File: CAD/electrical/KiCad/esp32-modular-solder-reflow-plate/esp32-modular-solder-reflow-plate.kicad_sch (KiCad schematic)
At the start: 58 parts, among them J4 TB003-500-P02BE, J5 I2C, J6 Micro_SD, J7 USB-C, SW1 µC_BTN01, SW2 µC_BTN02, SW3 µC_BTN03, SW4 µC_BTN04, SW5 µC_EN, SW6 µC_IO0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

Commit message: - CAD: schematic improvements
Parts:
- removed C10, C11, C13, C14, C15, C16: 1µ, Capacitor_SMD:C_0603_1608Metric_Pad1.08x0.95mm_HandSolder, symbol Device:C_Small
- removed C12, C17: 100n, Capacitor_SMD:C_0603_1608Metric_Pad1.08x0.95mm_HandSolder, symbol Device:C_Small
- removed C24: 10nF, Capacitor_SMD:C_0603_1608Metric, symbol Device:C
- removed C8: 100nF, Capacitor_SMD:C_0603_1608Metric, symbol Device:C
- removed C9: 4µ7, Capacitor_SMD:C_0603_1608Metric_Pad1.08x0.95mm_HandSolder, symbol Device:C_Small
- removed D11: SK6805, LED_SMD:LED_RGB_5050-6, symbol LED:SK6805
- removed D12: LED_B, LED_SMD:LED_0603_1608Metric_Pad1.05x0.95mm_HandSolder, symbol Device:LED
- removed D13: LED_GR, LED_SMD:LED_0603_1608Metric_Pad1.05x0.95mm_HandSolder, symbol Device:LED
- removed D14, D15, D16: LED_R, LED_SMD:LED_0603_1608Metric_Pad1.05x0.95mm_HandSolder, symbol Device:LED
- removed D3: REV_CUR_PROT, symbol Device:D_Schottky
- removed J4: TB003-500-P02BE, library_manager:SHDR2W100P0X500_1X2_1000X780X1030P, symbol library_loader:TB003-500-P02BE
- removed J5: I2C, Connector_PinSocket_2.54mm:PinSocket_1x05_P2.54mm_Vertical, symbol Connector_Generic:Conn_01x05
- removed J6: Micro_SD, Connector_Card:microSD_HC_Hirose_DM3D-SF, symbol Connector:Micro_SD_Card_Det
- removed J7: USB-C, Connector_USB:USB_C_Receptacle_GCT_USB4085, symbol Connector:USB_C_Receptacle_USB2.0
- removed L1: Ferrite bead, Inductor_SMD:L_0603_1608Metric_Pad1.05x0.95mm_HandSolder, symbol Device:L_Ferrite_Small
- removed R10, R17, R25: 10k, Resistor_SMD:R_0603_1608Metric_Pad0.98x0.95mm_HandSolder, symbol Device:R_Small
- removed R11, R12: 5k1, symbol Device:R_Small
- removed R13, R14, R15, R16, R27, R28, R29, R3, R5, R8, R9: 330, Resistor_SMD:R_0603_1608Metric_Pad0.98x0.95mm_HandSolder, symbol Device:R_Small
- removed R21, R22, R23, R24, R26: 0, Resistor_SMD:R_0603_1608Metric_Pad0.98x0.95mm_HandSolder, symbol Device:R_Small
- removed SW1: µC_BTN01, Button_Switch_THT:SW_PUSH_6mm, symbol Switch:SW_Push
- removed SW2: µC_BTN02, Button_Switch_THT:SW_PUSH_6mm, symbol Switch:SW_Push
- removed SW3: µC_BTN03, Button_Switch_THT:SW_PUSH_6mm, symbol Switch:SW_Push
- removed SW4: µC_BTN04, Button_Switch_THT:SW_PUSH_6mm, symbol Switch:SW_Push
- removed SW5: µC_EN, Button_Switch_THT:SW_PUSH_6mm, symbol Switch:SW_Push
- removed SW6: µC_IO0, Button_Switch_THT:SW_PUSH_6mm, symbol Switch:SW_Push
- added C2: 10n, symbol Device:C_Small
- added C6: 100n, symbol Device:C_Small
- added U1: ESP32-S3-WROOM-1, Espressif:ESP32-S3-WROOM-1, symbol espressif-kicad-lib:ESP32-S3-WROOM-1
- renumbered C26 to C1, C27 to C3, C28 to C4, C6 to C5, U4 to U3, Y2 to Y1
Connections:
- net FLASH is gone; now on net IO0: U3.27 (GPIO0/BOOT)
- net tempCS is gone; now on net ADC_TEMP_CS: U2.6 (~{CS})
- net tempSCK is gone; now on net ADC_TEMP_SCK: U2.5 (SCK)
- net tempSO is gone; now on net ADC_TEMP_SO: U2.7 (SO)
- net +3V3: now also C6.1; no longer U3.3 (EN)
- net ADC_TEMP_CS: now also U3.16 (GPIO46); no longer U3.31 (GPIO38/FSPIWP/SUBSPIWP)
- net ADC_TEMP_SCK: now also U3.25 (GPIO48/SPICLK_N/SUBSPICLK_N_DIFF)
- net ADC_TEMP_SO: now also U3.24 (GPIO47/SPICLK_P/SUBSPICLK_P_DIFF)
- net BTN01: now also U3.32 (MTCK/GPIO39/CLK_OUT3/SUBSPICS1)
- net BTN02: now also U3.33 (MTDO/GPIO40/CLK_OUT2)
- net BTN03: now also U3.34 (MTDI/GPIO41/CLK_OUT1)
- net BTN04: now also U3.35 (MTMS/GPIO42)
- net EN: now also U3.3 (EN)
- net GND: now also U3.1 (GND), U3.40 (GND), U3.41 (GND), C6.2
- net HEATER_CTRL: now also U3.12 (GPIO8/TOUCH8/ADC1_CH7/SUBSPICS1); no longer U3.18 (GPIO10/TOUCH10/ADC1_CH9/FSPICS0/FSPIIO4/SUBSPICS0)
- net I2C_SCL: now also U3.38 (GPIO2/TOUCH2/ADC1_CH1); no longer U3.15 (GPIO3/TOUCH3/ADC1_CH2)
- net I2C_SDA: now also U3.15 (GPIO3/TOUCH3/ADC1_CH2); no longer U3.4 (GPIO4/TOUCH4/ADC1_CH3)
- net LED_1: now also U3.6 (GPIO6/TOUCH6/ADC1_CH5); no longer U3.12 (GPIO8/TOUCH8/ADC1_CH7/SUBSPICS1)
- net LED_2: now also U3.7 (GPIO7/TOUCH7/ADC1_CH6); no longer U3.17 (GPIO9/TOUCH9/ADC1_CH8/FSPIHD/SUBSPIHD)
- net NEOPIXEL_DIN: now also U3.5 (GPIO5/TOUCH5/ADC1_CH4); no longer U3.7 (GPIO7/TOUCH7/ADC1_CH6)
- net SD_CD: now also U3.19 (GPIO11/TOUCH11/ADC2_CH0/FSPID/FSPIIO5/SUBSPID); no longer U3.21 (GPIO13/TOUCH13/ADC2_CH2/FSPIQ/FSPIIO7/SUBSPIQ)
- net SD_CLK: now also U3.20 (GPIO12/TOUCH12/ADC2_CH1/FSPICLK/FSPIIO6/SUBSPICLK); no longer U3.22 (GPIO14/TOUCH14/ADC2_CH3/FSPIWP/FSPIDQS/SUBSPIWP)
- net SD_CMD: now also U3.21 (GPIO13/TOUCH13/ADC2_CH2/FSPIQ/FSPIIO7/SUBSPIQ); no longer U3.10 (GPIO17/U1TXD/ADC2_CH6)
- net SD_DAT0: now also U3.22 (GPIO14/TOUCH14/ADC2_CH3/FSPIWP/FSPIDQS/SUBSPIWP); no longer U3.11 (GPIO18/U1RXD/ADC2_CH7/CLK_OUT3)
- net SD_DET: now also U3.18 (GPIO10/TOUCH10/ADC1_CH9/FSPICS0/FSPIIO4/SUBSPICS0); no longer U3.20 (GPIO12/TOUCH12/ADC2_CH1/FSPICLK/FSPIIO6/SUBSPICLK)
- net RX0: now reaches U3.36 (U0RXD/GPIO44/CLK_OUT2)
- net TX0: now reaches U3.37 (U0TXD/GPIO43/CLK_OUT1)
- net THCPL_p: now reaches U2.3 (T+)
- net THCPL_p: now also C2.2
- net THCPL_n: now reaches U2.2 (T-)
- net THCPL_n: now also C2.1
- net VccDiv: no longer names the net of U3.39 (GPIO1/TOUCH1/ADC1_CH0)
- new net: U1.1 (GND), U1.40 (GND), U1.41 (GND)
- no-connect marks 17 -> 8
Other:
- added sheet Input Output (input_output.kicad_sch)
- note removed: "BUTTONS"
- note removed: "CONNECTORS"
- note removed: "LEDS"
- note removed: "SD-CARD"
- title: (none) -> Modular Solder Reflow PCB

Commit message: - CAD: initial routed pcb
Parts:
- removed C3: 1µ, symbol Device:C_Small
- removed U1: ESP32-S3-WROOM-1, Espressif:ESP32-S3-WROOM-1, symbol espressif-kicad-lib:ESP32-S3-WROOM-1
- C1, C2: footprint (none) -> Capacitor_SMD:C_0603_1608Metric_Pad1.08x0.95mm_HandSolder
- C3: renamed from C4; footprint (none) -> Capacitor_SMD:C_0603_1608Metric_Pad1.08x0.95mm_HandSolder
- C4: renamed from C5; footprint (none) -> Capacitor_SMD:C_0603_1608Metric_Pad1.08x0.95mm_HandSolder
- C5: renamed from C6; footprint (none) -> Capacitor_SMD:C_0603_1608Metric_Pad1.08x0.95mm_HandSolder
- C6: renamed from C7; footprint (none) -> Capacitor_SMD:C_0603_1608Metric_Pad1.08x0.95mm_HandSolder
- Y1: footprint (none) -> Crystal:Crystal_SMD_3225-4Pin_3.2x2.5mm_HandSoldering
- renumbered U2 to U1, U3 to U2
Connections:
- net LED_1 is gone; now on net NEOPIXEL_DIN: U2.6 (GPIO6/TOUCH6/ADC1_CH5)
- net LED_2 is gone; now on net ADC_TEMP_SCK: U2.7 (GPIO7/TOUCH7/ADC1_CH6)
- net ADC_TEMP_CS: now also U2.10 (GPIO17/U1TXD/ADC2_CH6); no longer U2.16 (GPIO46)
- net ADC_TEMP_SCK: no longer U2.25 (GPIO48/SPICLK_N/SUBSPICLK_N_DIFF)
- net ADC_TEMP_SO: now also U2.11 (GPIO18/U1RXD/ADC2_CH7/CLK_OUT3); no longer U2.24 (GPIO47/SPICLK_P/SUBSPICLK_P_DIFF)
- net I2C_SCL: now also U2.5 (GPIO5/TOUCH5/ADC1_CH4); no longer U2.38 (GPIO2/TOUCH2/ADC1_CH1)
- net I2C_SDA: now also U2.4 (GPIO4/TOUCH4/ADC1_CH3); no longer U2.15 (GPIO3/TOUCH3/ADC1_CH2)
- net NEOPIXEL_DIN: no longer U2.5 (GPIO5/TOUCH5/ADC1_CH4)
- net RX0: now also U2.26 (GPIO45); no longer U2.36 (U0RXD/GPIO44/CLK_OUT2)
- net SD_CD: now also U2.18 (GPIO10/TOUCH10/ADC1_CH9/FSPICS0/FSPIIO4/SUBSPICS0); no longer U2.19 (GPIO11/TOUCH11/ADC2_CH0/FSPID/FSPIIO5/SUBSPID)
- net SD_CLK: now also U2.21 (GPIO13/TOUCH13/ADC2_CH2/FSPIQ/FSPIIO7/SUBSPIQ); no longer U2.20 (GPIO12/TOUCH12/ADC2_CH1/FSPICLK/FSPIIO6/SUBSPICLK)
- net SD_CMD: now also U2.20 (GPIO12/TOUCH12/ADC2_CH1/FSPICLK/FSPIIO6/SUBSPICLK); no longer U2.21 (GPIO13/TOUCH13/ADC2_CH2/FSPIQ/FSPIIO7/SUBSPIQ)
- net SD_DET: now also U2.19 (GPIO11/TOUCH11/ADC2_CH0/FSPID/FSPIIO5/SUBSPID); no longer U2.18 (GPIO10/TOUCH10/ADC1_CH9/FSPICS0/FSPIIO4/SUBSPICS0)
- net TX0: now also U2.25 (GPIO48/SPICLK_N/SUBSPICLK_N_DIFF); no longer U2.37 (U0TXD/GPIO43/CLK_OUT1)
- no-connect marks 8 -> 10
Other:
- moved on the sheet: C3, C4, C6, Y1

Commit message: - cad: improved routing; added VIN voltage monitoring capability
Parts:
- added R1: 100M, Resistor_SMD:R_0603_1608Metric_Pad0.98x0.95mm_HandSolder, symbol Device:R_Small
- added R2: 15M, Resistor_SMD:R_0603_1608Metric_Pad0.98x0.95mm_HandSolder, symbol Device:R_Small
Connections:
- net GND: now also R2.2
- net VIN_ADC: now reaches U2.15 (GPIO3/TOUCH3/ADC1_CH2)
- net VIN_ADC: now also R1.2, R2.1
- new net VCC_PWR: R1.1
- no-connect marks 10 -> 9
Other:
- note added: "Ensure to use appropriate voltage devider values!"
- note added: "VIN-Monitoring"
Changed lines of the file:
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@@
   (junction (at 67.31 143.51) (diameter 0) (color 0 0 0 0)
   )
+  (junction (at 109.22 165.1) (diameter 0) (color 0 0 0 0)
+  )
   (no_connect (at 127 52.07))
-  (no_connect (at 127 54.61))
   (no_connect (at 127 92.71))
   (no_connect (at 127 69.85))
@@
     (stroke (width 0) (type default))
   )
+  (wire (pts (xy 106.68 165.1) (xy 109.22 165.1))
+    (stroke (width 0) (type default))
+  )
+  (wire (pts (xy 109.22 167.64) (xy 109.22 165.1))
+    (stroke (width 0) (type default))
+  )
   (polyline (pts (xy 149.86 15.24) (xy 149.86 119.38))
     (stroke (width 0) (type default))
@@
     (stroke (width 0) (type default))
   )
+  (polyline (pts (xy 123.19 156.21) (xy 123.19 176.53))
+    (stroke (width 0) (type default))
+  )
   (wire (pts (xy 30.48 177.8) (xy 30.48 180.34))
     (stroke (width 0) (type default))
@@
     (stroke (width 0) (type default))
   )
+  (wire (pts (xy 99.06 165.1) (xy 101.6 165.1))
+    (stroke (width 0) (type default))
+  )
   (wire (pts (xy 62.23 128.27) (xy 67.31 128.27))
     (stroke (width 0) (type default))
@@
     (stroke (width 0) (type default))
   )
+  (polyline (pts (xy 123.19 176.53) (xy 85.09 176.53))
+    (stroke (width 0) (type default))
+  )
   (polyline (pts (xy 82.55 156.21) (xy 15.24 156.21))
     (stroke (width 0) (type default))
@@
     (stroke (width 0) (type default))
   )
+  (wire (pts (xy 127 54.61) (xy 129.54 54.61))
+    (stroke (width 0) (type default))
+  )
   (wire (pts (xy 33.02 41.91) (xy 35.56 41.91))
     (stroke (width 0) (type default))
@@
     (stroke (width 0) (type default))
   )
+  (wire (pts (xy 109.22 165.1) (xy 111.76 165.1))
+    (stroke (width 0) (type default))
+  )
   (polyline (pts (xy 15.24 153.67) (xy 15.24 121.92))
     (stroke (width 0) (type default))
@@
     (stroke (width 0) (type default))
   )
+  (wire (pts (xy 116.84 165.1) (xy 119.38 165.1))
+    (stroke (width 0) (type default))
+  )
   (wire (pts (xy 41.91 162.56) (xy 41.91 163.83))
     (stroke (width 0) (type default))
@@
     (stroke (width 0) (type default))
   )
+  (polyline (pts (xy 85.09 156.21) (xy 123.19 156.21))
+    (stroke (width 0) (type default))
+  )
   (wire (pts (xy 127 74.93) (xy 129.54 74.93))
     (stroke (width 0) (type default))
@@
     (stroke (width 0) (type default))
   )
+  (wire (pts (xy 119.38 165.1) (xy 119.38 167.64))
+    (stroke (width 0) (type default))
+  )
   (polyline (pts (xy 15.24 15.24) (xy 15.24 119.38))
     (stroke (width 0) (type default))
@@
     (stroke (width 0) (type default))
   )
+  (wire (pts (xy 99.06 167.64) (xy 109.22 167.64))
+    (stroke (width 0) (type default))
+  )
   (wire (pts (xy 33.02 24.13) (xy 81.28 24.13))
+    (stroke (width 0) (type default))
+  )
+  (polyline (pts (xy 85.09 156.21) (xy 85.09 176.53))
     (stroke (width 0) (type default))
   )
@@
     (effects (font (size 1.27 1.27)) (justify left bottom))
   )
+  (text "Ensure to use appropriate \nvoltage devider values!" (exclude_from_sim no)
+    (at 88.9 173.99 0)
+    (effects (font (size 1.27 1.27) (thickness 0.254) bold (color 255 0 13 1)) (justify left bottom))
+  )
   (text "µC-PASSIVES\n" (exclude_from_sim no)
  (at 17.78 125.73 0)
     (effects (font (size 1.27 1.27) (thickness 0.254) bold) (justify left bottom))
   )
+  (text "VIN-Monitoring\n" (exclude_from_sim no)
+ (at 87.63 160.02 0)
+    (effects (font (size 1.27 1.27) (thickness 0.254) bold) (justify left bottom))
+  )
   (text "µC\n" (exclude_from_sim no)
  (at 17.78 19.05 0)
@@
     )
   )
+  (global_label "VIN_ADC" (shape output) (at 99.06 167.64 180) (fields_autoplaced)
+    (effects (font (size 1.27 1.27)) (justify right))
+    (property "Intersheetrefs" "${INTERSHEET_REFS}" (at 88.5341 167.64 0)
+      (effects (font (size 1.27 1.27)) (justify right) hide)
+    )
+  )
   (global_label "BTN03" (shape input) (at 33.02 52.07 180) (fields_autoplaced)
     (effects (font (size 1.27 1.27)) (justify right))
@@
     )
   )
+  (global_label "VCC_PWR" (shape input) (at 99.06 165.1 180) (fields_autoplaced)
+    (effects (font (size 1.27 1.27)) (justify right))
+    (property "Intersheetrefs" "${INTERSHEET_REFS}" (at 87.5666 165.1 0)
+      (effects (font (size 1.27 1.27)) (justify right) hide)
+    )
+  )
   (global_label "XTAL_P" (shape bidirectional) (at 57.15 134.62 180) (fields_autoplaced)
     (effects (font (size 1.27 1.27)) (justify right))
@@
     (effects (font (size 1.27 1.27)) (justify left))
     (property "Intersheetrefs" "${INTERSHEET_REFS}" (at 140.4286 82.55 0)
+      (effects (font (size 1.27 1.27)) (justify left) hide)
+    )
+  )
+  (global_label "VIN_ADC" (shape input) (at 129.54 54.61 0) (fields_autoplaced)
+    (effects (font (size 1.27 1.27)) (justify left))
+    (property "Intersheetrefs" "${INTERSHEET_REFS}" (at 140.0659 54.61 0)
       (effects (font (size 1.27 1.27)) (justify left) hide)
     )
@@
     )
   )
+  (symbol (lib_id "Device:R_Small") (at 104.14 165.1 90) (unit 1)
+    (in_bom yes) (on_board yes) (dnp no)
+    (property "Reference" "R1" (at 101.6 162.56 90)
+      (effects (font (size 1.27 1.27)))
+    )
+    (property "Value" "100M" (at 106.68 162.56 90)
+      (effects (font (size 1.27 1.27)))
+    )
+    (property "Footprint" "Resistor_SMD:R_0603_1608Metric_Pad0.98x0.95mm_HandSolder" (at 104.14 165.1 0)
+      (effects (font (size 1.27 1.27)) hide)
+    )
+    (property "Datasheet" "~" (at 104.14 165.1 0)
+      (effects (font (size 1.27 1.27)) hide)
+    )
+    (pin "1")
+    (pin "2")
+    (instances
+      (project "esp32-modular-solder-reflow-plate"
+        (path "/33f3a99a-8df0-41a5-be2d-1e3400ca68bb"
+          (reference "R1") (unit 1)
+        )
+        (path "/33f3a99a-8df0-41a5-be2d-1e3400ca68bb/9103847b-7285-41f5-846d-96de7eb793c2"
+          (reference "R?") (unit 1)
+        )
+      )
+      (project "dspctl_esp32_r0"
+        (path "/8b3186b5-4efc-4a83-b981-ca6a69ceeadc"
+          (reference "R?") (unit 1)
+        )
+        (path "/8b3186b5-4efc-4a83-b981-ca6a69ceeadc/5662498d-5991-4f3b-8484-1c94b706ac61"
+          (reference "R?") (unit 1)
+        )
+      )
+    )
+  )
+  (symbol (lib_id "Device:R_Small") (at 114.3 165.1 90) (unit 1)
+    (in_bom yes) (on_board yes) (dnp no)
+    (property "Reference" "R2" (at 113.03 162.56 90)
+      (effects (font (size 1.27 1.27)))
+    )
+    (property "Value" "15M" (at 118.11 162.56 90)
+      (effects (font (size 1.27 1.27)))
+    )
+    (property "Footprint" "Resistor_SMD:R_0603_1608Metric_Pad0.98x0.95mm_HandSolder" (at 114.3 165.1 0)
+      (effects (font (size 1.27 1.27)) hide)
+    )
+    (property "Datasheet" "~" (at 114.3 165.1 0)
+      (effects (font (size 1.27 1.27)) hide)
+    )
+    (pin "1")
+    (pin "2")
+    (instances
+      (project "esp32-modular-solder-reflow-plate"
+        (path "/33f3a99a-8df0-41a5-be2d-1e3400ca68bb"
+          (reference "R2") (unit 1)
+        )
+        (path "/33f3a99a-8df0-41a5-be2d-1e3400ca68bb/9103847b-7285-41f5-846d-96de7eb793c2"
+          (reference "R?") (unit 1)
+        )
+      )
+      (project "dspctl_esp32_r0"
+        (path "/8b3186b5-4efc-4a83-b981-ca6a69ceeadc"
+          (reference "R?") (unit 1)
+        )
+        (path "/8b3186b5-4efc-4a83-b981-ca6a69ceeadc/5662498d-5991-4f3b-8484-1c94b706ac61"
+          (reference "R?") (unit 1)
+        )
+      )
+    )
+  )
   (symbol (lib_id "power:GND") (at 62.23 129.54 0) (unit 1)
     (in_bom yes) (on_board yes) (dnp no)
@@
         )
       )
+    )
+  )
+  (symbol (lib_id "power:GND") (at 119.38 167.64 0) (unit 1)
+    (in_bom yes) (on_board yes) (dnp no)
+    (property "Reference" "#PWR09" (at 119.38 173.99 0)
+      (effects (font (size 1.27 1.27)) hide)
+    )
+    (property "Value" "GND" (at 119.38 171.45 0)
+      (effects (font (size 1.27 1.27)))
+    )
+    (property "Footprint" "" (at 119.38 167.64 0)
+      (effects (font (size 1.27 1.27)) hide)
+    )
+    (property "Datasheet" "" (at 119.38 167.64 0)
+      (effects (font (size 1.27 1.27)) hide)
+    )
+    (pin "1")
+    (instances
+      (project "esp32-modular-solder-reflow-plate"
+        (path "/33f3a99a-8df0-41a5-be2d-1e3400ca68bb"
+          (reference "#PWR09") (unit 1)
+        )
+        (path "/33f3a99a-8df0-41a5-be2d-1e3400ca68bb/9103847b-7285-41f5-846d-96de7eb793c2"
+          (reference "#PWR?") (unit 1)
+        )
+      )

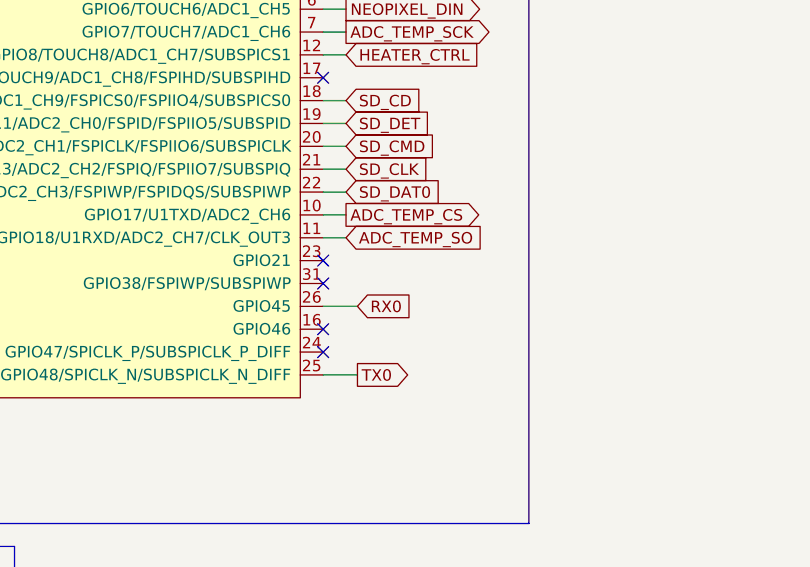
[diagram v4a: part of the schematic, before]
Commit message: - cad: added a buzzer control output
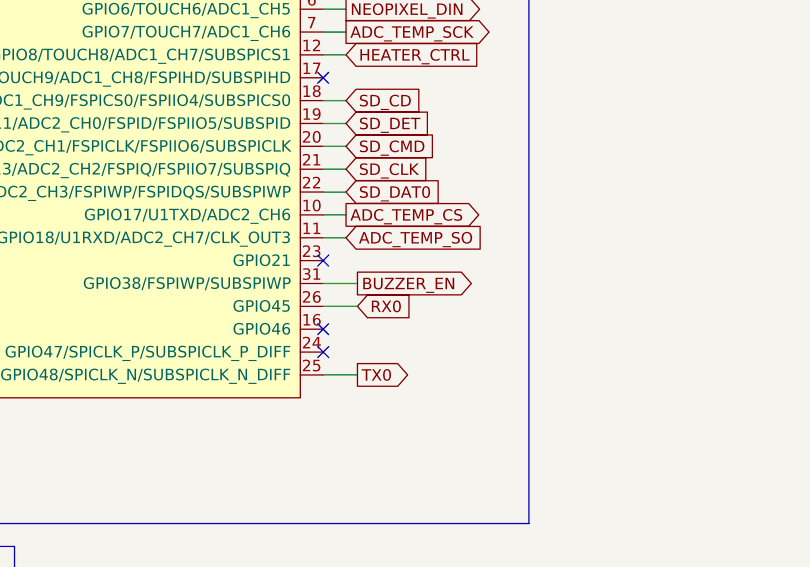
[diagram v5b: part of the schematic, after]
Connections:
- net BUZZER_EN: now reaches U2.31 (GPIO38/FSPIWP/SUBSPIWP)
- no-connect marks 9 -> 8
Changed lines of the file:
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@@
   )
   (no_connect (at 127 52.07))
-  (no_connect (at 127 92.71))
   (no_connect (at 127 69.85))
   (no_connect (at 127 34.29))
@@
     (stroke (width 0) (type default))
   )
+  (wire (pts (xy 127 92.71) (xy 130.81 92.71))
+    (stroke (width 0) (type default))
+  )
   (wire (pts (xy 77.47 143.51) (xy 77.47 142.24))
     (stroke (width 0) (type default))
@@
       (effects (font (size 1.27 1.27)) (justify left) hide)
     )
+  )
+  (global_label "BUZZER_EN" (shape output) (at 130.81 92.71 0) (fields_autoplaced)
+    (effects (font (size 1.27 1.27)) (justify left))
+    (property "Intersheetrefs" "${INTERSHEET_REFS}" (at 144.6014 92.71 0)
+      (effects (font (size 1.27 1.27)) (justify left) hide)
+    )
